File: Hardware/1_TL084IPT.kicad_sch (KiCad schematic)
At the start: 23 parts, among them J7 Screw_Terminal_01x08, Q1 N_Mosfet, Q2 N_Mosfet, Q20 N_Mosfet, Q3 N_Mosfet, U11 TL084

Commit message: layout part 2
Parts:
- D10, D11, D8, D9: footprint IVS_FOOTPRINTS:D_MiniMELF -> IVS_FOOTPRINTS:D_SOD323
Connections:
- net VAN1_output: now also R44.2, U11.7; no longer R43.2, U11.1
- net VAN2_output: now also R43.2, U11.1; no longer R44.2, U11.7
- net VAN3_output: now also R46.2, U11.14; no longer R45.2, U11.8
- net VAN4_output: now also R45.2, U11.8; no longer R46.2, U11.14
- net at Q20.2 (S), R35.1: now also U11.5 (+); no longer U11.3 (+)
- net at Q2.2 (S), R37.1: now also U11.12 (+); no longer U11.10 (+)
- net at Q3.2 (S), R38.1: now also U11.10 (+); no longer U11.12 (+)
- net at Q1.2 (S), R36.1: now also U11.3 (+); no longer U11.5 (+)
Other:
- moved on the sheet: R43, R44, R45, R46, U11A, U11B, U11C, U11D

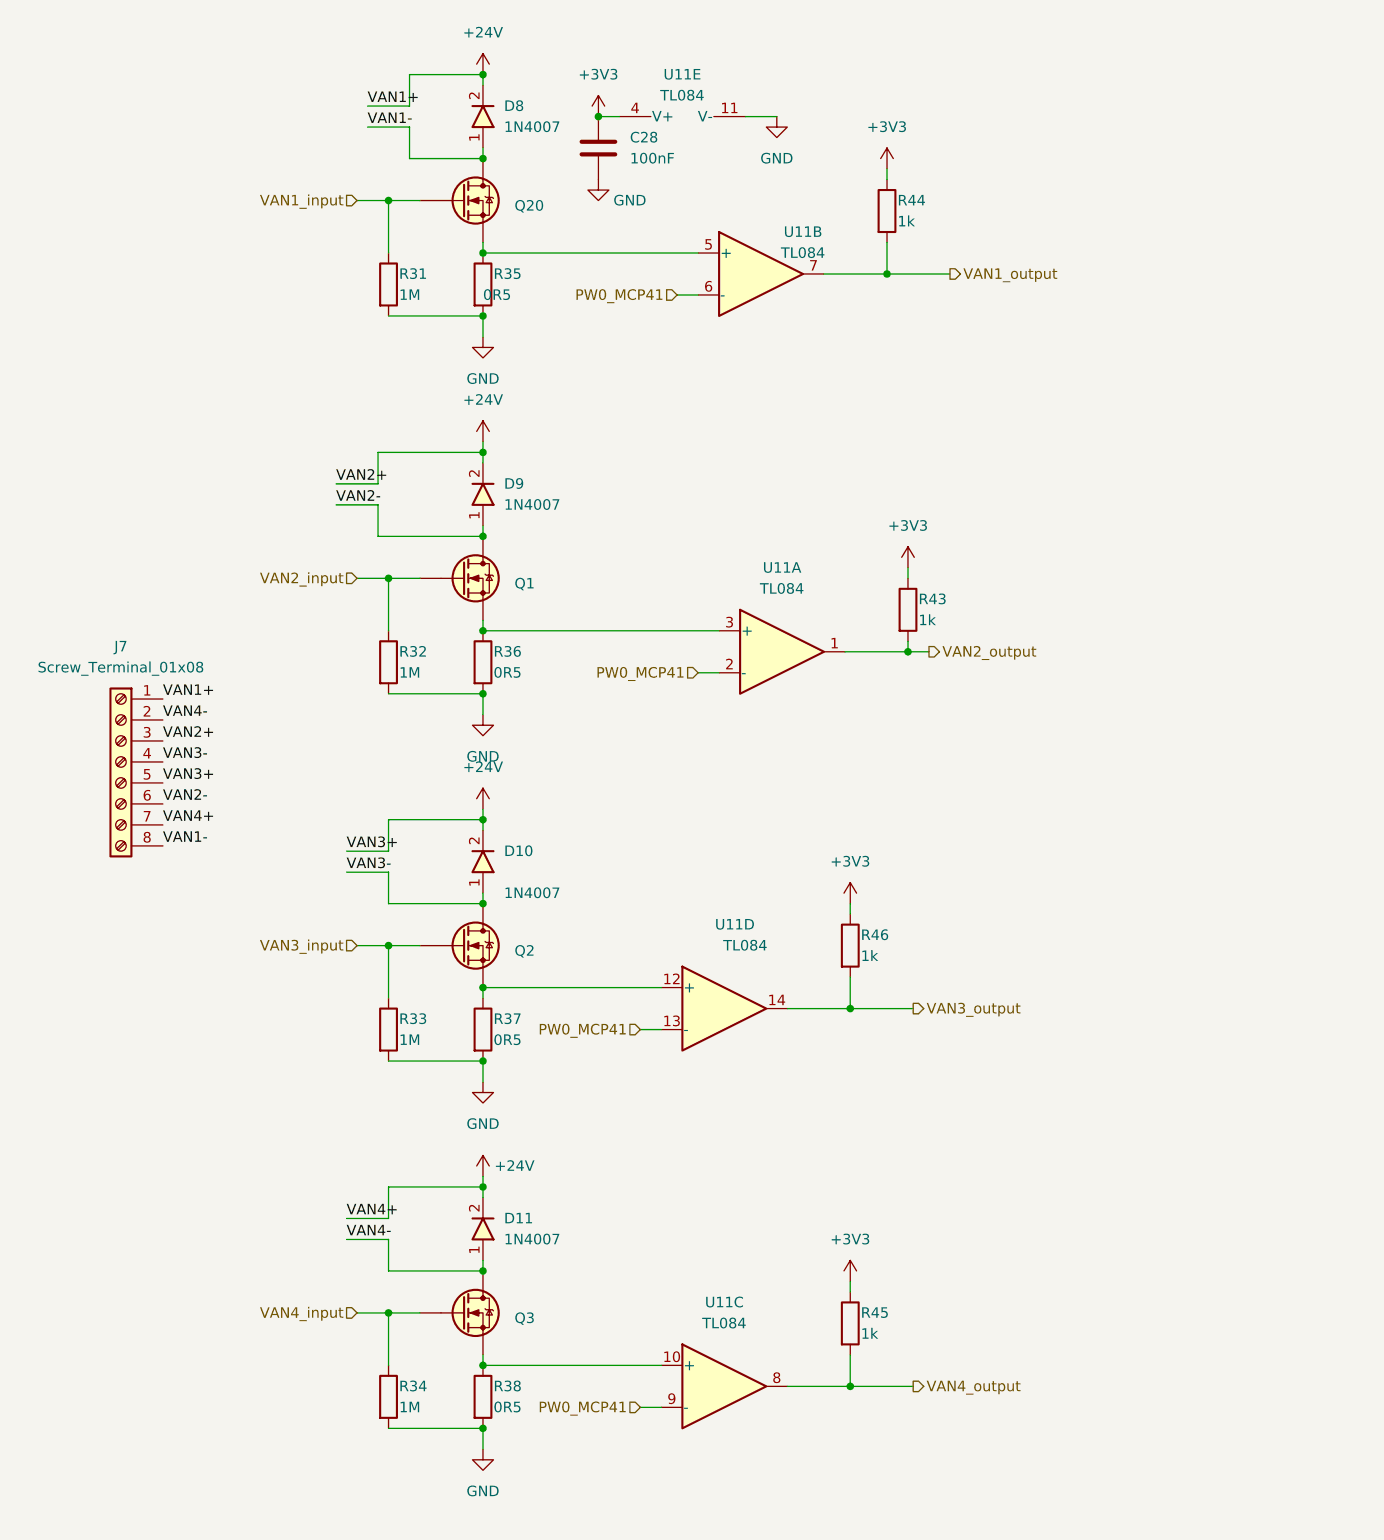
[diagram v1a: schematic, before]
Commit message: add lora, relay, opto, opamp block, led for 74595. Delete RT9193, connect boot0,1 to GND. Fix footprint crystal 8M, 74HC595, IDC pin
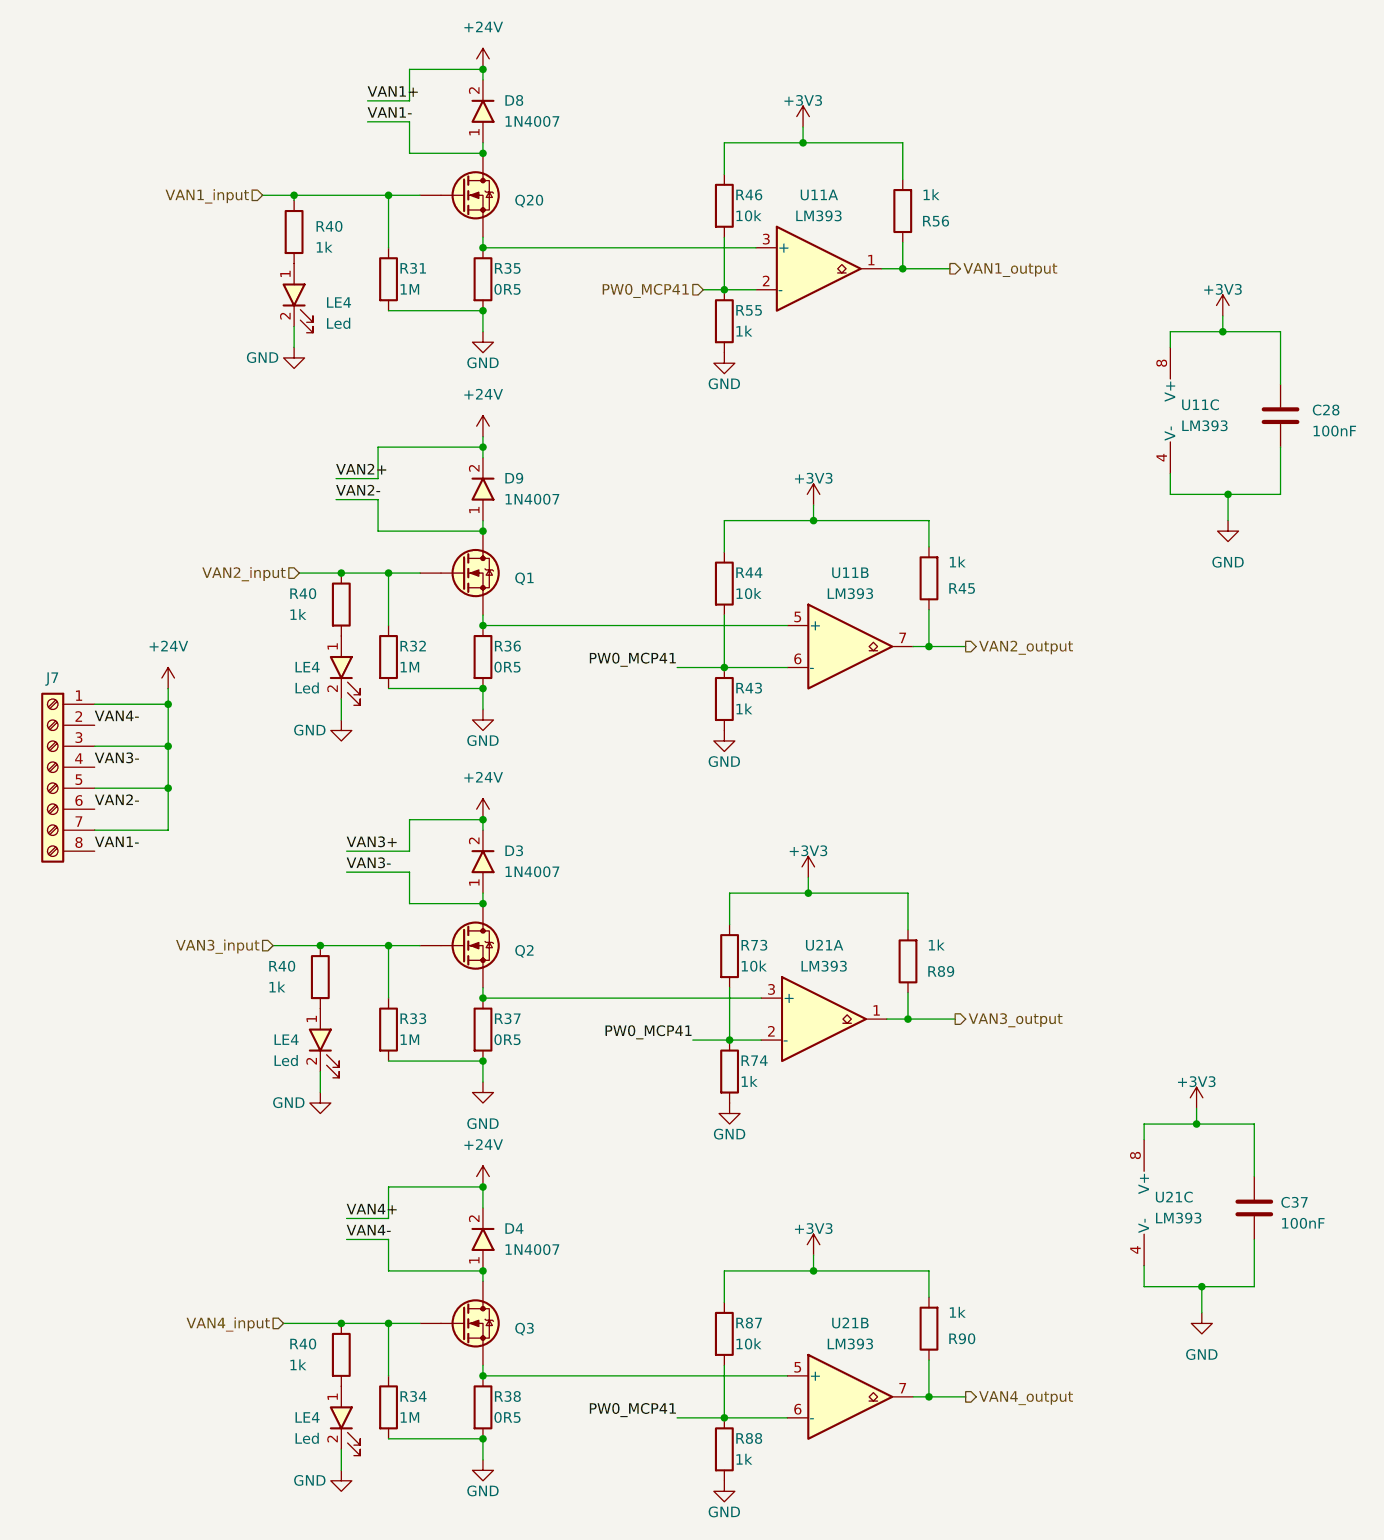
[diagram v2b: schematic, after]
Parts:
- removed D10, D11: 1N4007, IVS_FOOTPRINTS:D_SOD323, symbol IVS_SYMBOL_DIR:D_Diode
- removed U11: TL084, IVS_FOOTPRINTS:TSSOP14, symbol Amplifier_Operational:TL084
- added C37: 100nF, IVS_FOOTPRINTS:C_0603, symbol Device:C
- added D3, D4: 1N4007, IVS_FOOTPRINTS:D_SOD323, symbol IVS_SYMBOL_DIR:D_Diode
- added LE4 (x4): Led, IVS_FOOTPRINTS:LED_0603, symbol IVS_SYMBOLS:Led
- added R40 (x4), R55, R56, R74, R88, R89, R90: 1k, IVS_FOOTPRINTS:R_0603, symbol Device:R
- added R73, R87: 10k, IVS_FOOTPRINTS:R_0603, symbol Device:R
- added U11, U21: LM393, IVS_FOOTPRINTS:SOIC-8_3.9x4.9mm_P1.27mm, symbol Comparator:LM393
- C28: footprint IVS_FOOTPRINTS:C0603 -> IVS_FOOTPRINTS:C_0603
- R31, R32, R33, R34, R43, R45: footprint IVS_FOOTPRINTS:R0603 -> IVS_FOOTPRINTS:R_0603
- R35, R36, R37, R38: footprint Resistor_SMD:R_0805_2012Metric -> IVS_FOOTPRINTS:R_0805
- R44, R46: value 1k -> 10k; footprint IVS_FOOTPRINTS:R0603 -> IVS_FOOTPRINTS:R_0603
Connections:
- net +24V: now also D3.2, D4.2
- net +3V3: now also R45.2, C37.1, R56.2, R73.1, R87.1, R89.2, R90.2, U11.8 (V+), U21.8 (V+); no longer R43.1, R45.1
- net GND: now also R43.2, C37.2, LE4.2, LE4.2, LE4.2, LE4.2, R55.2, R74.2, R88.2, U11.4 (V-), U21.4 (V-)
- net PW0_MCP41: now also R43.1, R44.2, R46.2, R55.1, R73.2, R74.1, R87.2, R88.1, U11.2 (-), U11.6 (-), U21.2 (-), U21.6 (-)
- net VAN1_input: now also R40.1
- net VAN1_output: now also R56.1, U11.1; no longer R44.2
- net VAN2_input: now also R40.1
- net VAN2_output: now also R45.1, U11.7; no longer R43.2
- net VAN3-: now also D3.1
- net VAN3_input: now also R40.1
- net VAN3_output: now also R89.1, U21.1; no longer R46.2
- net VAN4-: now also D4.1
- net VAN4_input: now also R40.1
- net VAN4_output: now also R90.1, U21.7; no longer R45.2
- net at Q1.2 (S), R36.1: now also U11.5 (+)
- net at Q2.2 (S), R37.1: now also U21.3 (+)
- net at Q3.2 (S), R38.1: now also U21.5 (+)
- net at Q20.2 (S), R35.1: now also U11.3 (+)
- new net: LE4.1, R40.2 (x4)
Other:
- moved on the sheet: D8, D9, J7, Q1, Q20, R31, R32, R35, R36
